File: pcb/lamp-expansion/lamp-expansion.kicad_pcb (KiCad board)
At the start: 2 copper layers, 96 parts, among them IC1 78L05_SOT, IC10 74HC4050, IC2 MCP73811, IC3 AP2411, IC4 LM2623_VSSOP, IC5 LM1117_3.3, IC6 LM1117_5.0, IC7 FT230X_SOP, IC8 TLV1117LV28, IC9 CC3000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

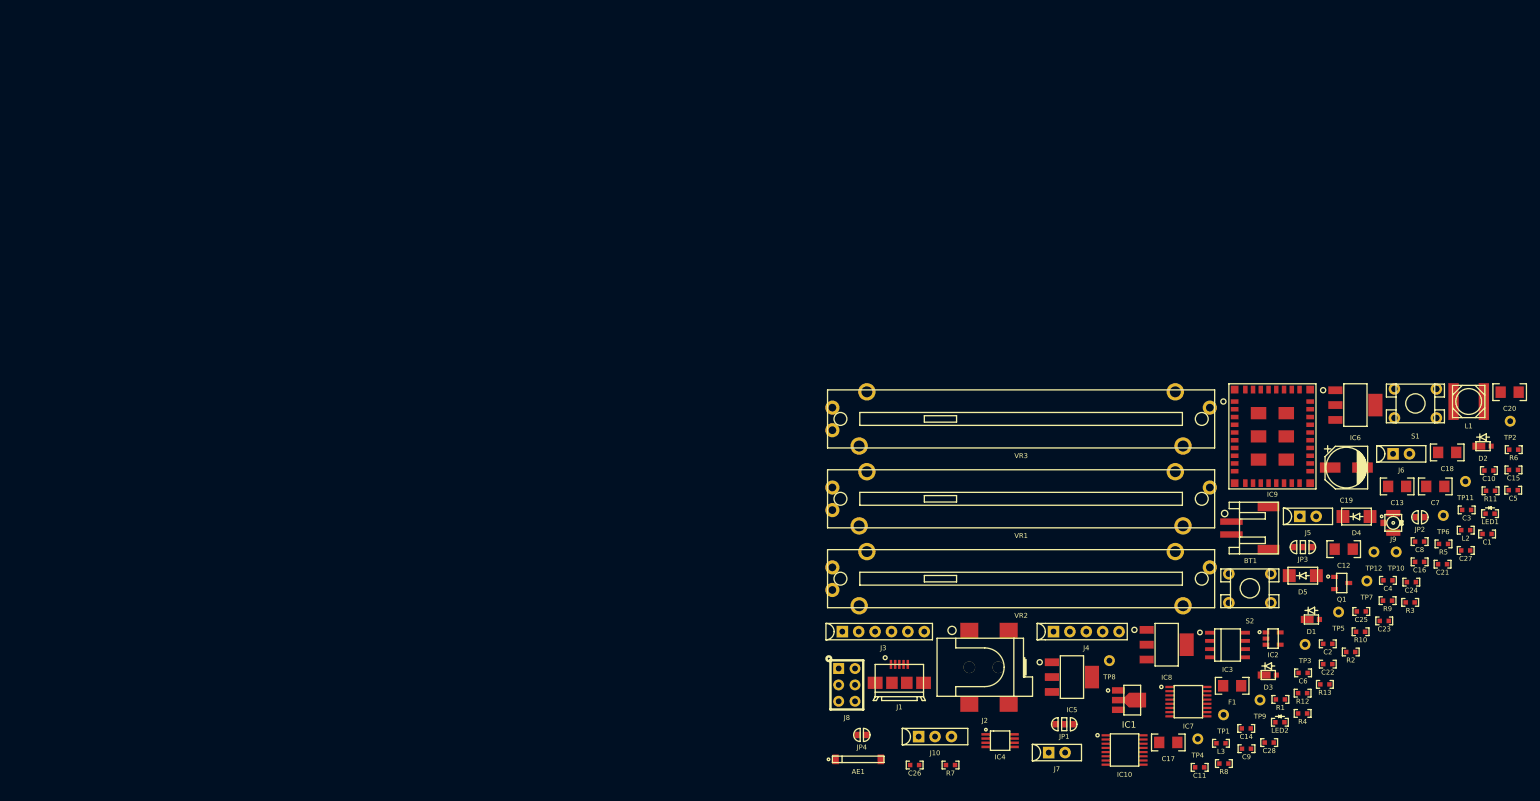
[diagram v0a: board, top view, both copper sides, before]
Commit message: replace boost regulator
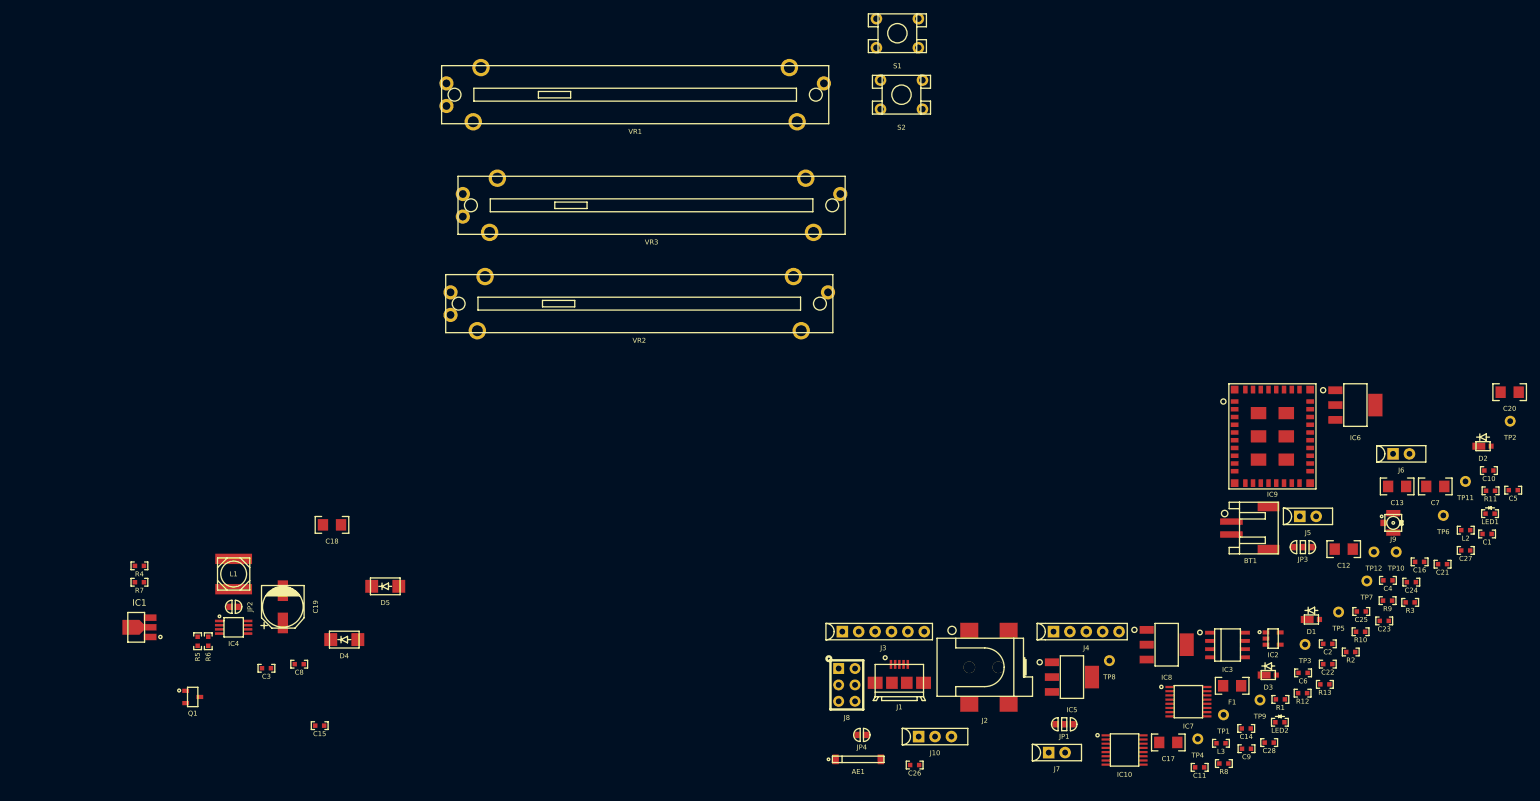
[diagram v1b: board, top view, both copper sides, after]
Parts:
- moved R6 204.5 mm to (65.3, 120.9), turned to 90 degrees
- moved R5 193.7 mm to (63.6, 120.9), turned to 270 degrees
- moved L1 193.3 mm to (69.2, 110.5), turned to 270 degrees
- moved C15 189.2 mm to (82.5, 134.0)
- moved C3 187.6 mm to (74.3, 125.1)
- moved JP2 184.4 mm to (69.2, 115.6), turned to 180 degrees
- moved R4 181.7 mm to (54.6, 109.2)
- moved Q1 179.0 mm to (62.9, 129.5)
- moved C8 174.7 mm to (79.4, 124.5)
- moved C18 173.2 mm to (84.5, 102.9)
- moved C19 166.2 mm to (76.8, 115.6), turned to 90 degrees
- moved D4 158.0 mm to (86.4, 120.7)
- moved IC1 153.8 mm to (54.6, 118.7), turned to 180 degrees
- moved D5 142.2 mm to (92.7, 112.4)
- moved R7 128.9 mm to (54.6, 111.8)
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
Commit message: working on the layout;
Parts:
- removed IC4: LM2623_VSSOP, sop:VSSOP8_P0.65mm_W3mm
- added C29: 2.2nF, passive-smd:0603(1608m), F.Cu at (54.0, 125.1)
- added C30: 0.1uF, passive-smd:0603(1608m), F.Cu at (58.4, 120.7)
- added C31: 10uF, passive-smd:1206(3216m), F.Cu at (62.2, 121.9)
- C15: value 4.7pF -> 1uF
- C18: value 22uF -> 47pF; footprint passive-smd:1206(3216m) -> passive-smd:0603(1608m)
- C3: value 0.1uF -> 100uF; footprint passive-smd:0603(1608m) -> capacitor:PANA-D_CHEMI-F_SM-ALUMINUM
- C8: value 0.1uF -> 10uF; footprint passive-smd:0603(1608m) -> passive-smd:1206(3216m)
- IC1: value 78L05_SOT -> PAM2421; footprint sot:SOT89 -> sop:SOP8_ep
- L1: value 4.7uH -> 6.8uH; footprint inductor:SM-INDUCTOR_5mmX5mm -> inductor:SM-INDUCTOR_6mmX6mm
- R5: value 91kΩ -> 10kΩ
- R6: value 430kΩ -> 47kΩ
- R7: value 150kΩ -> 51k
- moved C20 167.5 mm to (109.9, 140.3), turned to 90 degrees
- moved C13 159.1 mm to (96.5, 140.3), turned to 90 degrees
- moved C1 156.0 mm to (110.5, 134.6), turned to 270 degrees
- moved IC6 150.4 mm to (103.5, 140.3)
- moved BT1 130.7 mm to (99.1, 130.8), turned to 180 degrees
- moved IC2 123.8 mm to (107.3, 134.6), turned to 90 degrees
- moved IC3 114.3 mm to (109.2, 129.5)
- moved C9 113.8 mm to (112.4, 134.6), turned to 90 degrees
- moved IC7 90.3 mm to (134.0, 95.2)
- moved JP1 83.1 mm to (114.9, 129.5), turned to 270 degrees
- moved D5 55.9 mm to (38.1, 124.5), turned to 180 degrees
- moved C18 43.0 mm to (47.6, 125.1), turned to 180 degrees
- moved J1 43.0 mm to (134.0, 108.0)
- moved C15 37.9 mm to (47.6, 119.4), turned to 270 degrees
- moved C3 35.7 mm to (39.4, 117.5), turned to 90 degrees
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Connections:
- C15 pad 1: Net-(C15-Pad1) -> GND
- C15 pad 2: Net-(C15-Pad2) -> VCC
- C18 pad 1: VCC -> Net-(C18-Pad1)
- C3 pad 1: GND -> VCC
- C3 pad 2: Net-(C3-Pad2) -> GND
- C8 pad 1: /V_LED -> VCC
- D4 pad 2: VCC -> Net-(D4-Pad2)
- IC1 pad 1: Net-(C3-Pad2) -> GND
- IC1 pad 2: GND -> VCC
- IC1 pad 3: /V_LED -> Net-(IC1-Pad3)
- JP2 pad 1: Net-(C15-Pad2) -> VCC
- JP2 pad 2: Net-(C15-Pad2) -> VCC
- L1 pad 1: VCC -> Net-(D4-Pad2)
- L1 pad 2: Net-(C15-Pad2) -> VCC
- Q1 pad 3: Net-(IC4-Pad2) -> Net-(IC1-Pad3)
- R4 pad 1: Net-(IC4-Pad2) -> VCC
- R4 pad 2: Net-(C3-Pad2) -> Net-(IC1-Pad3)
- R5 pad 1: Net-(IC4-Pad4) -> Net-(IC1-Pad6)
- R6 pad 1: /V_LED -> Net-(IC1-Pad6)
- R6 pad 2: Net-(IC4-Pad4) -> /V_LED
- R7 pad 1: Net-(C15-Pad1) -> Net-(C18-Pad1)
- R7 pad 2: VCC -> Net-(C29-Pad2)
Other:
- net class Default: clearance 0.254 -> 0.2032; trace_width 0.254 -> 0.2032; via_dia 0.889 -> 0.762; via_drill 0.635 -> 0.381
- rule pad_to_mask_clearance: 0 -> 0.0762
- rule trace_clearance: 0.254 -> 0.2032
- rule trace_min: 0.254 -> 0.1524
- rule via_min_drill: 0.508 -> 0.3302
- rule via_min_size: 0.889 -> 0.6858

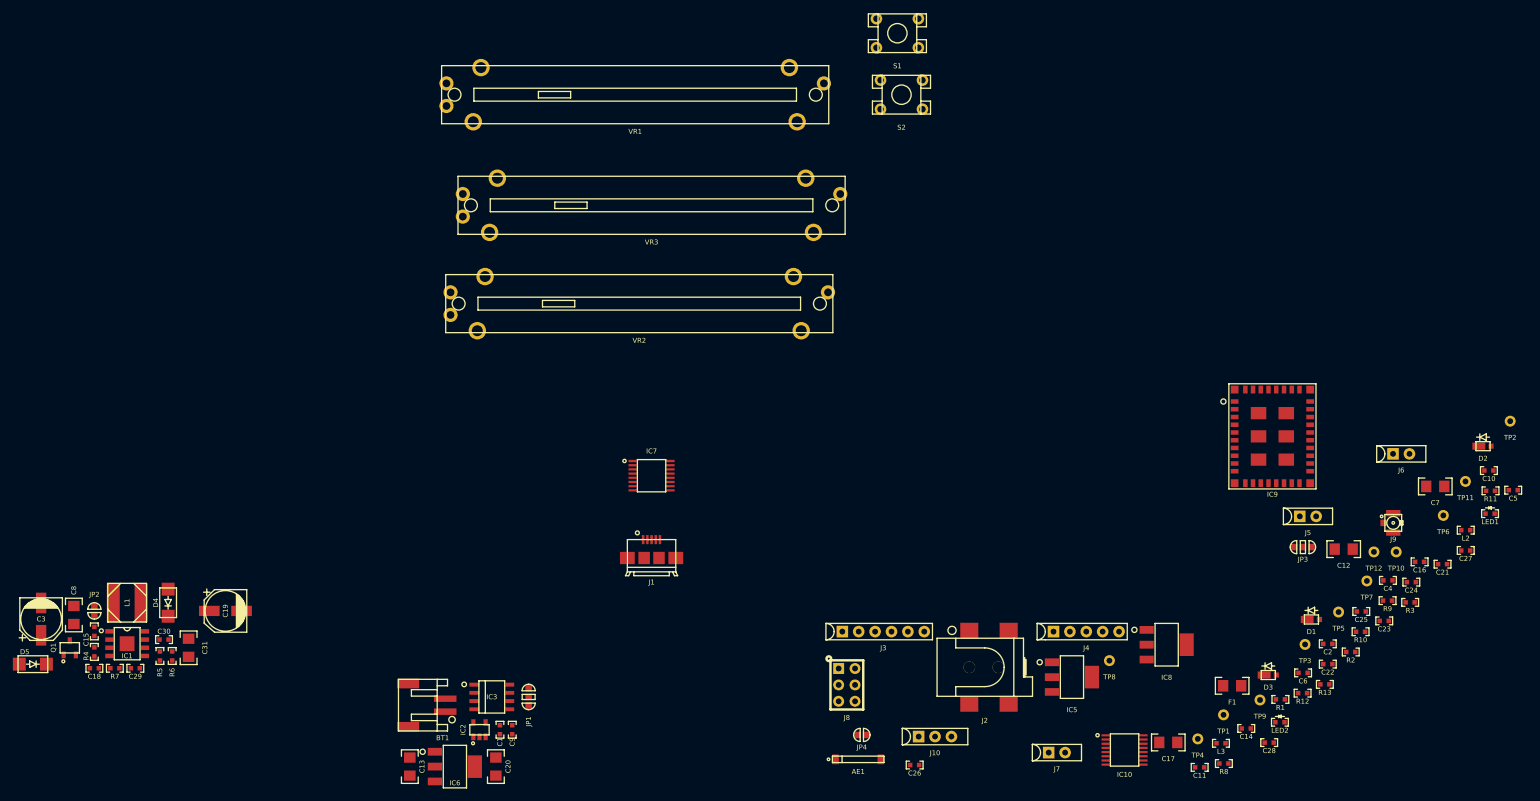
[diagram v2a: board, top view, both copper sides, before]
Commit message: modules grouped in layout;
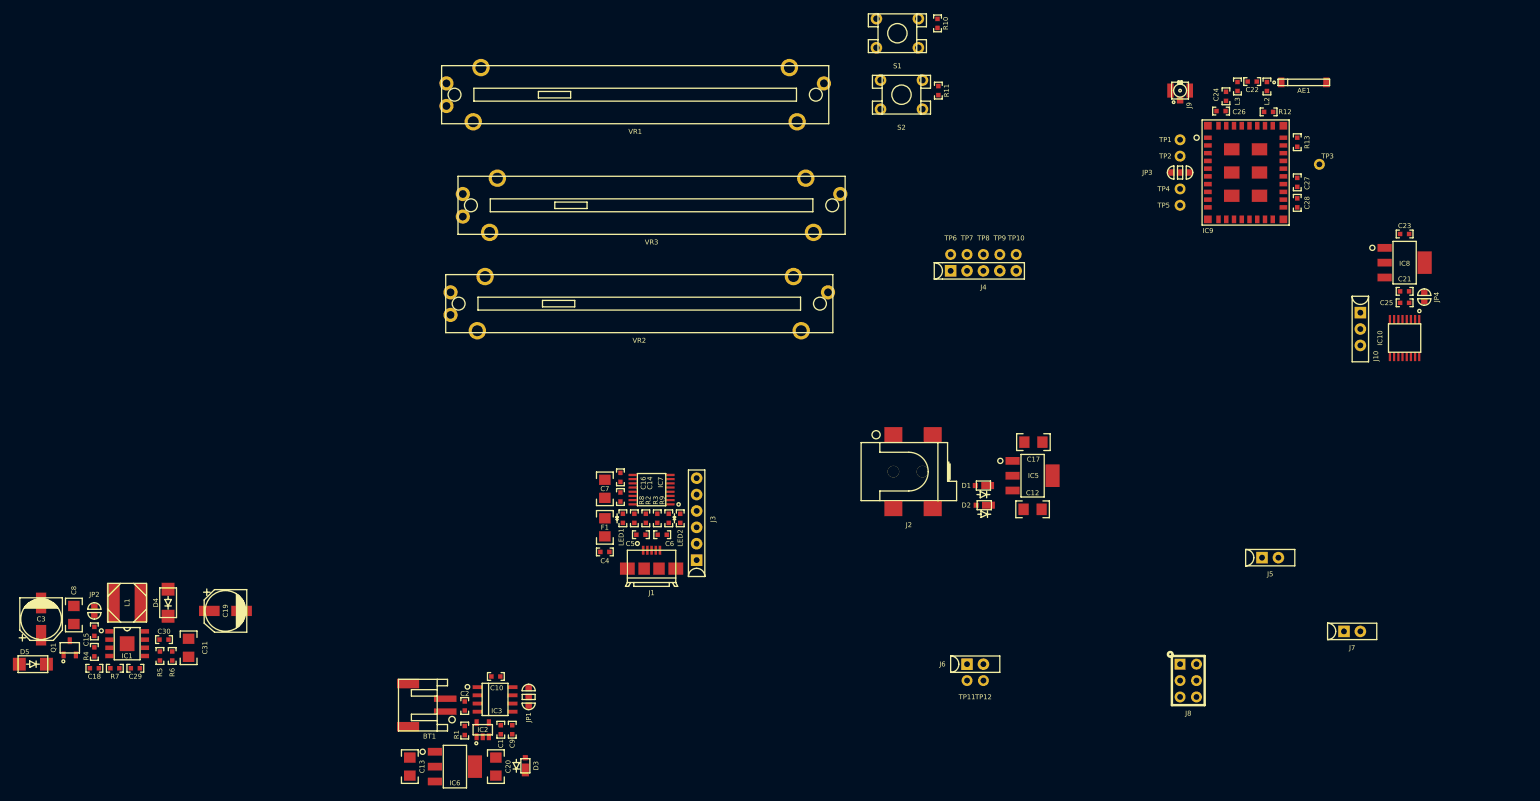
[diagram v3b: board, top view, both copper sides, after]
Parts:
- removed C11: 0.1uF, passive-smd:0603(1608m)
- moved C10 157.2 mm to (109.9, 126.4), turned to 180 degrees
- moved C5 135.4 mm to (132.3, 104.4), turned to 180 degrees
- moved LED1 134.4 mm to (129.5, 101.9), turned to 90 degrees
- moved C2 134.1 mm to (105.0, 130.9), turned to 270 degrees
- moved C7 128.7 mm to (126.7, 97.3), turned to 270 degrees
- moved R1 126.5 mm to (105.0, 134.7), turned to 90 degrees
- moved AE1 125.6 mm to (235.1, 34.3)
- moved C16 124.3 mm to (129.2, 98.6), turned to 270 degrees
- moved C4 121.4 mm to (126.7, 107.1), turned to 180 degrees
- moved R3 117.4 mm to (134.9, 101.9), turned to 90 degrees
- moved D3 116.0 mm to (114.4, 140.2), turned to 90 degrees
- moved R10 114.8 mm to (178.3, 25.1), turned to 90 degrees
- moved R9 112.1 mm to (136.7, 101.9), turned to 270 degrees
- moved C26 111.9 mm to (222.2, 38.7), turned to 180 degrees
- moved R2 111.2 mm to (133.1, 101.9), turned to 90 degrees
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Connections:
- IC7 pad 16: (no net) -> Net-(IC7-Pad16)
- IC7 pad 6: Net-(IC7-Pad6) -> /USB_CTS

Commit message: board layout and schematic refinement
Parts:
- removed C12: 10uF, passive-smd:1206(3216m)
- removed C17: 22uF, passive-smd:1206(3216m)
- removed C21, C23: 1uF, passive-smd:0603(1608m)
- removed C25: 0.1uF, passive-smd:0603(1608m)
- removed D5: 3A, diode:DO-214AC
- removed IC10: 74HC4050, sop:TSSOP16
- removed IC5: LM1117_3.3, sot:SOT223
- removed IC8: TLV1117LV28, sot:SOT223
- removed J10: CC-IO, sip:SIP3
- removed J6: 2PIN_IO, sip:SIP2
- removed JP1: VBAT-DIR-SEL, jumper:SOLDER-JUMPER_2-WAY
- removed JP2: I-TEST, jumper:SOLDER-JUMPER_1-WAY
- removed JP4: WIFI-LOG-LVL-SEL, jumper:SOLDER-JUMPER_1-WAY
- removed TP11, TP12: PIN, connect-thru:1-PIN
- added D6: 2A, diode:MICROSMP, F.Cu at (81.2, 97.2)
- added Q2: 2N7002, sot:SOT23, F.Cu at (79.6, 108.6)
- D1, D3: value MSS2P2 -> 3A; footprint diode:MICROSMP -> diode:DO-214AC
- D2: value MSS2P2 -> 2A
- IC3: value AP2411 -> AP2411_ep; footprint soic:SOIC8 -> sop:MSOP8_ep
- J2: footprint connect-sm:CUI-PJ-002AH-SMT_dc-barrel-jack -> connect-thru:CUI-PJ-102A_dc-barrel-jack
- moved J7 184.2 mm to (58.4, 125.1), turned to 180 degrees
- moved J5 172.0 mm to (58.4, 121.9), turned to 180 degrees
- moved D2 112.2 mm to (73.7, 91.3), turned to 90 degrees
- moved D1 111.7 mm to (74.2, 106.7), turned to 0 degrees
- moved J2 92.9 mm to (81.0, 90.6), turned to 30 degrees
- moved J8 63.8 mm to (230.1, 64.5)
- moved C20 55.4 mm to (67.3, 104.8), turned to 180 degrees
- moved LED2 54.3 mm to (85.3, 113.3), turned to 180 degrees
- moved C14 54.0 mm to (82.2, 122.0), turned to 270 degrees
- moved R8 53.7 mm to (83.4, 126.1), turned to 0 degrees
- moved IC7 53.2 mm to (85.7, 119.8), turned to 270 degrees
- moved R9 53.0 mm to (85.3, 115.1), turned to 0 degrees
- moved J3 52.4 mm to (94.0, 125.1), turned to 0 degrees
- moved LED1 51.3 mm to (83.4, 124.5), turned to 180 degrees
- moved C16 51.2 mm to (82.2, 119.0), turned to 90 degrees
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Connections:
- C10 pad 1: VCC -> /VSUP
- C13 pad 1: /V_DC -> Net-(C13-Pad1)
- C15 pad 2: VCC -> /VSUP
- C27 pad 1: /V_IO -> VCC
- C3 pad 1: VCC -> /VSUP
- C8 pad 1: VCC -> /VSUP
- D1 pad 1: /V_DC -> /VSUP
- D1 pad 2: /DC_IN -> +5V
- D2 pad 1: /V_DC -> Net-(C13-Pad1)
- D2 pad 2: /V_USB -> /DC_IN
- IC1 pad 2: VCC -> /VSUP
- IC3 pad 4: +5V -> Net-(IC3-Pad4)
- IC3 pad 6: VCC -> /VSUP
- IC3 pad 7: VCC -> /VSUP
- IC3 pad 8: VCC -> /VSUP
- IC6 pad 3: /V_DC -> Net-(C13-Pad1)
- IC9 pad 23: /V_IO -> VCC
- J4 pad 1: /POT_0 -> /CC_IRQ
- J4 pad 2: /POT_1 -> /SW_1
- J4 pad 3: /POT_2 -> /POT_0
- J4 pad 4: /SW_0 -> /CC_EN
- J4 pad 5: /SW_1 -> /CC_SEL
- J7 pad 1: VCC -> /VSUP
- J8 pad 3: /AVR_SCK -> /CC_SCK
- J8 pad 4: /AVR_MOSI -> /CC_MOSI
- L1 pad 2: VCC -> /VSUP
- R1 pad 1: GND -> +BATT
- R1 pad 2: +5V -> Net-(IC3-Pad4)
- R10 pad 2: /SW_0 -> /CC_IRQ
- R4 pad 1: VCC -> /VSUP
- S1 pad 2: /SW_0 -> /CC_IRQ
- TP10 pad 1: /SW_1 -> /CC_SEL
- TP6 pad 1: /POT_0 -> /CC_IRQ
- TP7 pad 1: /POT_1 -> /SW_1
- TP8 pad 1: /POT_2 -> /POT_0
- TP9 pad 1: /SW_0 -> /CC_EN
- VR2 pad 2: /POT_1 -> /CC_EN
- VR3 pad 2: /POT_2 -> /CC_SEL
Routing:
- net GND: track 0.00 -> 150.1 mm, vias 0 -> 6
- net /VSUP: track 0.00 -> 67.4 mm, vias 0 -> 4
- net /DC_IN: track 0.00 -> 56.1 mm, vias 0 -> 1
- net /V_LED: track 0.00 -> 50.3 mm, vias 0 -> 2
- net +5V: track 0.00 -> 49.9 mm, vias 0 -> 2
- net /V_USB: track 0.00 -> 24.8 mm, vias 0 -> 3
- net /V_FTDI: track 0.00 -> 23.8 mm, vias 0 -> 2
- net /USB_RTS: track 0.00 -> 20.6 mm, vias 0 -> 1
- net +BATT: track 0.00 -> 20.1 mm
- net /USB_RX: track 0.00 -> 18.8 mm, vias 0 -> 1
- net Net-(D4-Pad2): track 0.00 -> 17.1 mm
- net /USB_CTS: track 0.00 -> 14.4 mm, vias 0 -> 1
- net Net-(IC7-Pad14): track 0.00 -> 14.4 mm, vias 0 -> 2
- net /USB_TX: track 0.00 -> 12.7 mm, vias 0 -> 1
- net Net-(C4-Pad2): track 0.00 -> 12.1 mm
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- added copper zone on B.Cu, net GND
- added copper zone on F.Cu, net GND
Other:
- board outline added: 53.3 x 46.2 mm
